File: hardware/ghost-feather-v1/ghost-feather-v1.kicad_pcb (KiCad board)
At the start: 4 copper layers, 72 parts, among them J1 Conn_ARM_SWD_TagConnect_TC2030, J2 USB_C_Receptacle_USB2.0, J3 Conn_01x03, J4 Conn_01x03, J5 Conn_01x03, J6 Conn_01x03, J7 Conn_01x08, Q1 BSS138, Q2 BSS138, Q3 BSS138, Q4 BSS138, SW2 BOOT0, U1 STM32F722RETx, U2 BMI270, U3 USBLC6-2SC6_MOD, U4 MPM3610, U5 MPM3610, X1 16MHz, X2 32kHz768

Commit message: feat: Components placement on PCB #2
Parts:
- moved J5 99.0 mm to (177.0, 53.8)
- moved J6 93.3 mm to (106.7, 57.7)
- moved C14 81.1 mm to (108.0, 53.3)
- moved C17 80.3 mm to (108.7, 124.5)
- moved J4 76.5 mm to (170.5, 130.1)
- moved Q4 68.7 mm to (114.6, 58.2)
- moved R8 68.4 mm to (178.6, 57.7)
- moved Q1 66.4 mm to (113.5, 124.5)
- moved C18 61.1 mm to (118.4, 66.5)
- moved R5 60.3 mm to (110.7, 54.1)
- moved C19 59.0 mm to (121.9, 66.8)
- moved R17 57.0 mm to (105.9, 97.8)
- moved D2 56.3 mm to (124.7, 75.9)
- moved R14 56.3 mm to (108.5, 121.2)
- moved C10 56.2 mm to (125.7, 106.9)
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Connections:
- U1 pad 35: /RF_CH5 -> /RF_CH0
- U1 pad 36: /RF_CH4 -> /RF_CH1
- U1 pad 37: /RF_CH0 -> /RF_CH2
- U1 pad 38: /RF_CH1 -> /RF_CH3
- U1 pad 39: /RF_CH2 -> /RF_CH4
- U1 pad 40: /RF_CH3 -> /RF_CH5

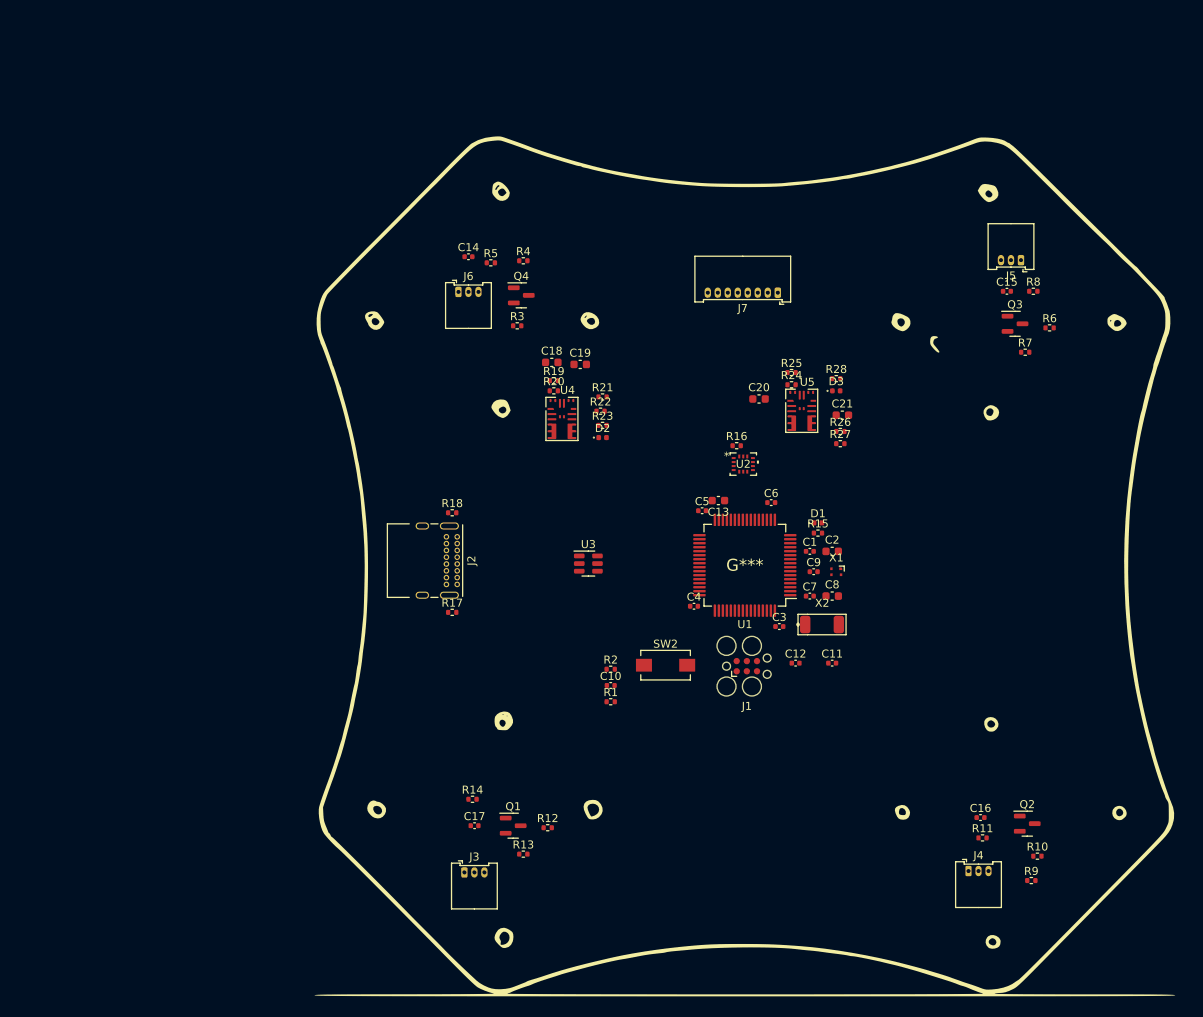
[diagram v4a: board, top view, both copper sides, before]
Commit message: feat: Components placement on PCB #3
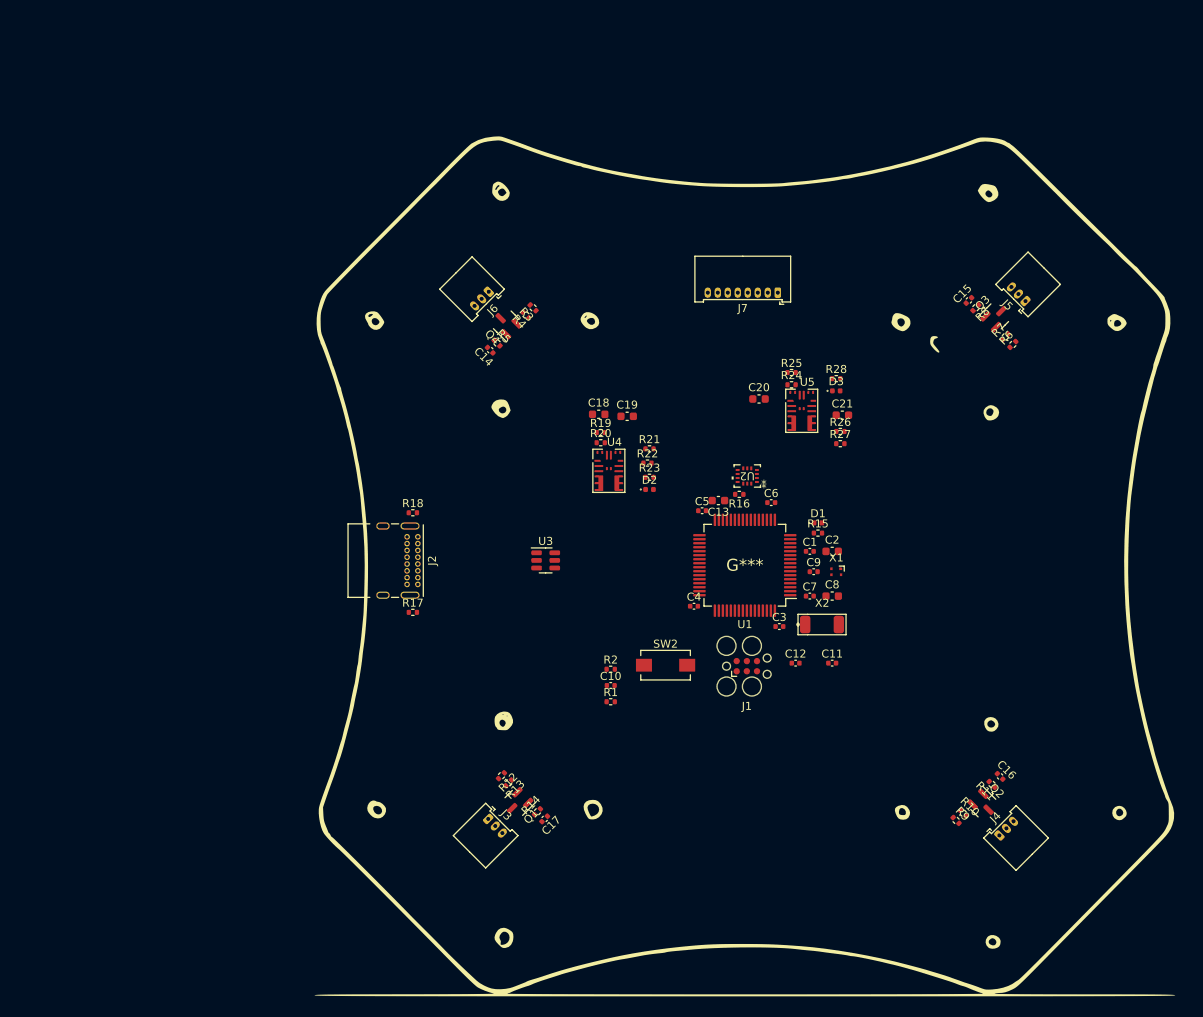
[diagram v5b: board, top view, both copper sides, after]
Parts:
- moved R9 12.0 mm to (168.9, 123.8), turned to -45 degrees
- moved C14 12.0 mm to (110.7, 65.0), turned to 135 degrees
- moved R10 10.7 mm to (169.8, 122.9), turned to -45 degrees
- moved R5 10.1 mm to (111.5, 64.1), turned to -45 degrees
- moved R13 9.09 mm to (113.0, 119.1), turned to -135 degrees
- moved C17 8.81 mm to (117.5, 123.6), turned to -135 degrees
- moved D2 8.75 mm to (130.6, 82.4)
- moved R21 8.75 mm to (130.6, 77.4)
- moved R23 8.75 mm to (130.6, 80.9)
- moved C18 8.75 mm to (124.2, 73.0)
- moved R20 8.75 mm to (124.5, 76.6)
- moved U4 8.75 mm to (125.5, 80.4)
- moved C19 8.75 mm to (127.8, 73.3)
- moved R19 8.75 mm to (124.5, 75.3)
- moved R22 8.75 mm to (130.3, 79.1)
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
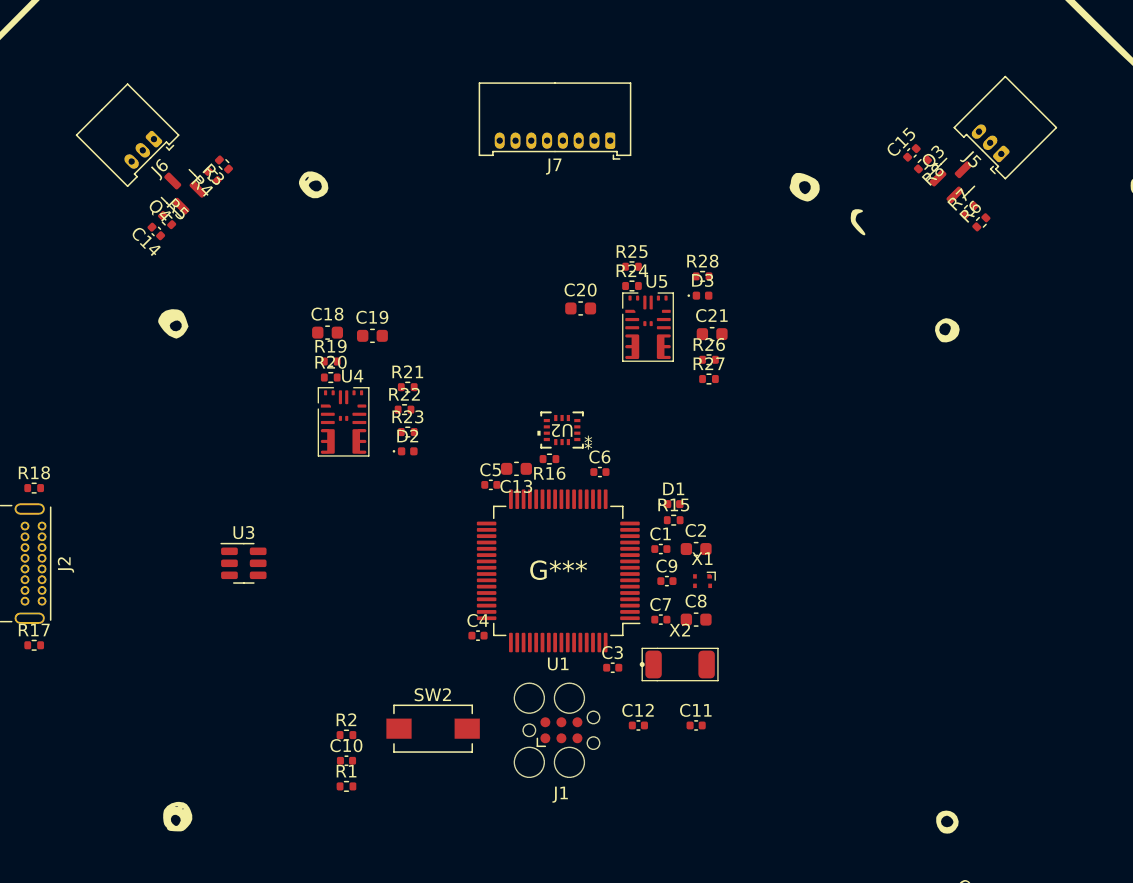
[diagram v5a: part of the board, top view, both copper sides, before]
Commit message: feat: Components placement on PCB #4
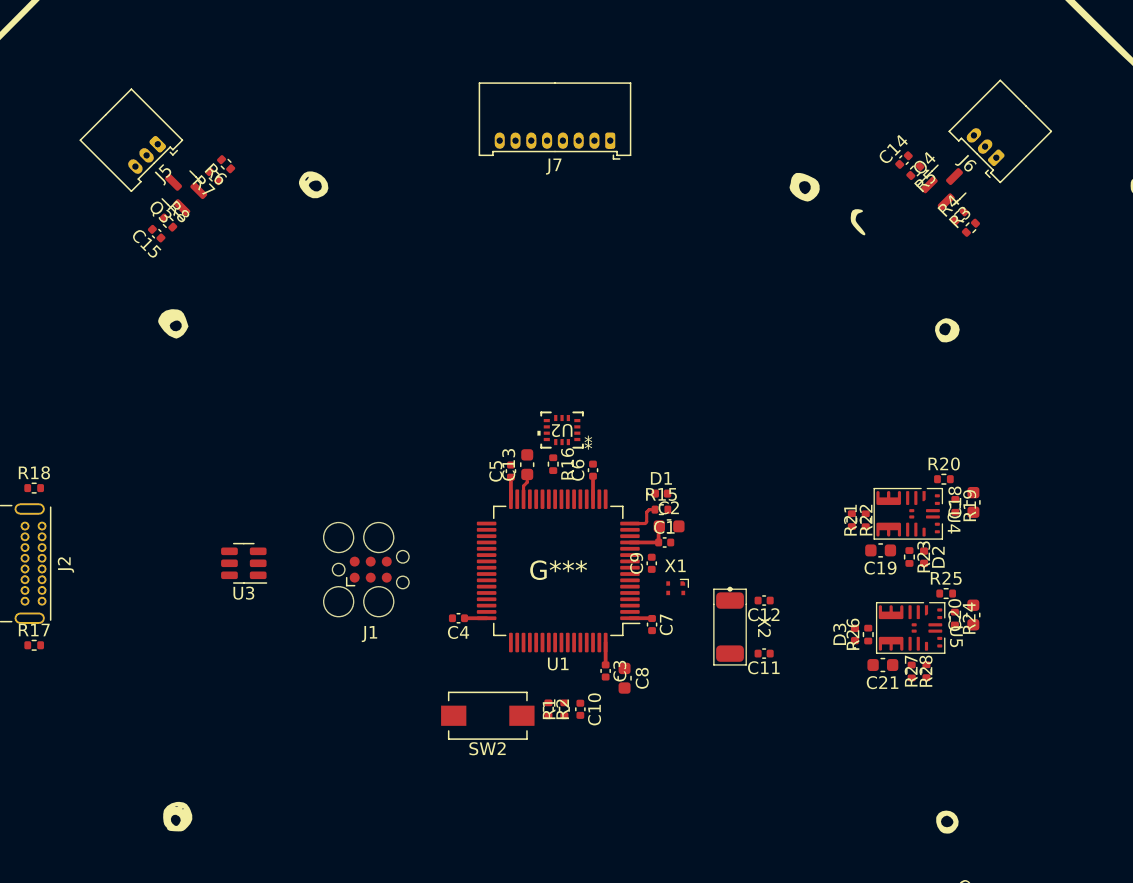
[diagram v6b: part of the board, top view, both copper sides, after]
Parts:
- moved J5 66.8 mm to (110.8, 58.1), turned to -135 degrees
- moved J6 66.7 mm to (177.2, 59.2), turned to 135 degrees
- moved Q3 61.2 mm to (112.7, 61.8), turned to 135 degrees
- moved Q4 60.6 mm to (173.2, 61.3), turned to 45 degrees
- moved C15 60.1 mm to (110.7, 65.2), turned to 135 degrees
- moved R6 60.0 mm to (116.2, 59.7), turned to 135 degrees
- moved R8 59.9 mm to (111.6, 64.3), turned to -45 degrees
- moved R7 59.9 mm to (115.2, 60.6), turned to 135 degrees
- moved C14 59.5 mm to (169.9, 59.4), turned to 45 degrees
- moved R5 59.4 mm to (170.8, 60.2), turned to -135 degrees
- moved R3 59.4 mm to (175.2, 64.7), turned to 45 degrees
- moved R4 59.2 mm to (174.3, 63.8), turned to 45 degrees
- moved C18 52.9 mm to (175.4, 86.5), turned to 90 degrees
- moved R19 50.8 mm to (173.9, 86.8), turned to -90 degrees
- moved R20 49.2 mm to (173.0, 84.6)
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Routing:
- net +3V3: track 0.00 -> 12.4 mm
- net /LED_USER: track 0.00 -> 2.89 mm
- net Net-(U1-VCAP_1): track 0.00 -> 2.08 mm

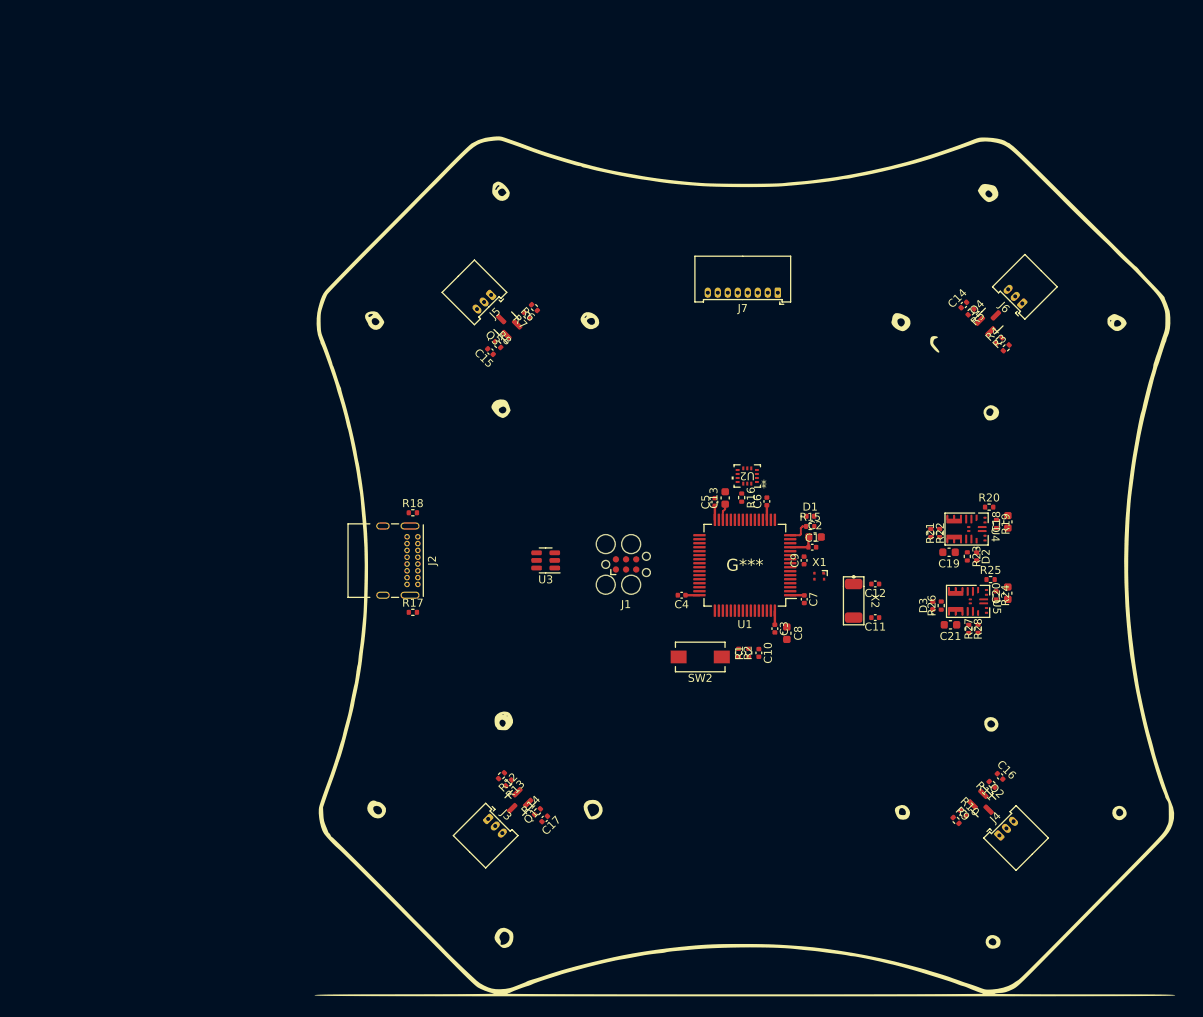
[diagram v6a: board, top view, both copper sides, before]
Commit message: feat: Add the PCB edge cut layer
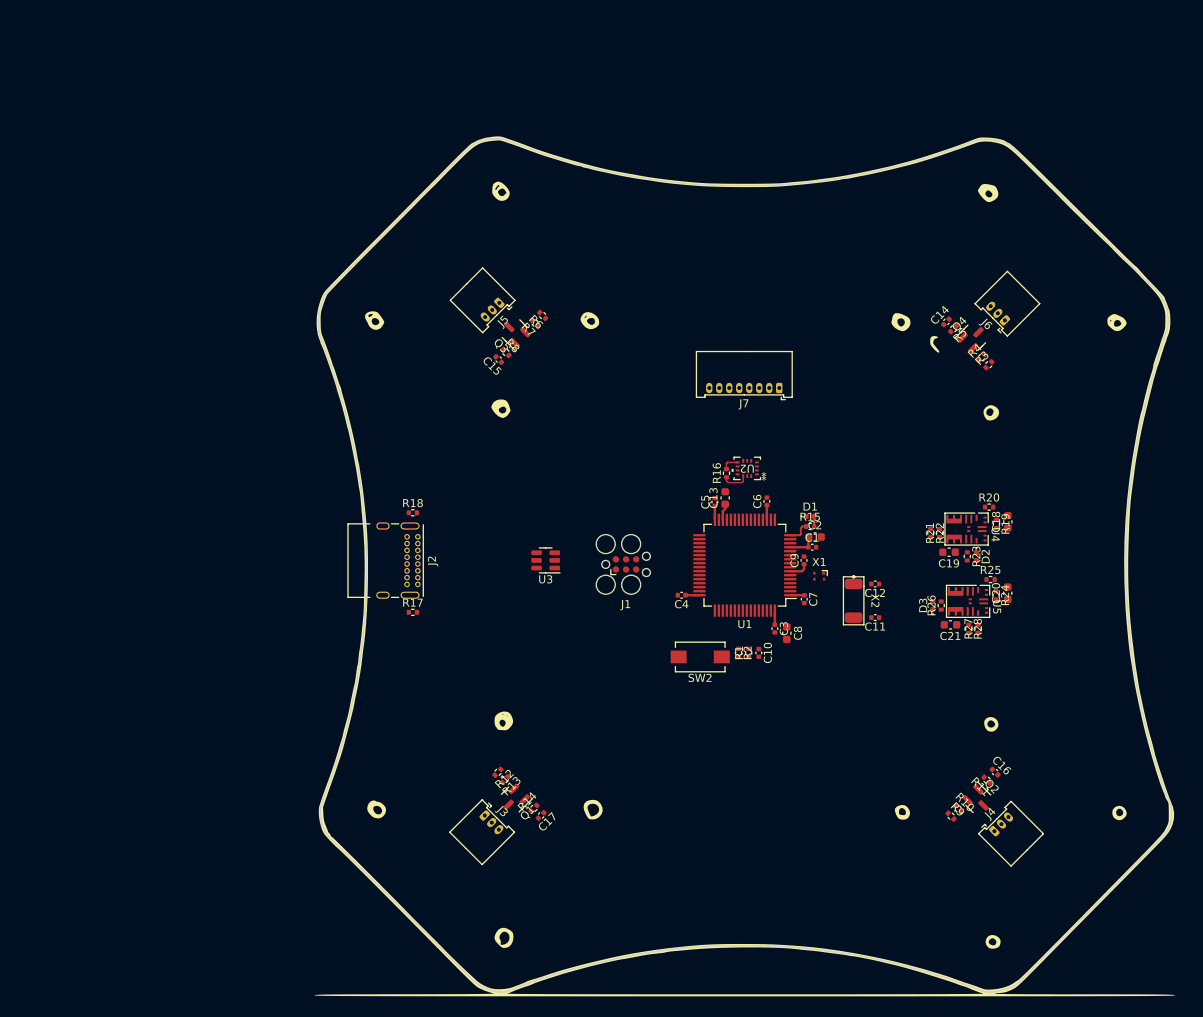
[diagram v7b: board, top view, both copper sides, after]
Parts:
- moved J7 11.9 mm to (146.8, 69.8)
- moved R16 3.59 mm to (140.2, 80.4), turned to 90 degrees
- moved R5 3.03 mm to (168.6, 62.3)
- moved C14 3.03 mm to (167.7, 61.5)
- moved J6 3.03 mm to (175.0, 61.3)
- moved Q4 3.03 mm to (171.0, 63.4)
- moved R3 3.03 mm to (173.0, 66.8)
- moved R4 3.03 mm to (172.1, 65.9)
- moved R8 1.43 mm to (112.6, 65.3)
- moved Q3 1.43 mm to (113.7, 62.8)
- moved R6 1.43 mm to (117.2, 60.7)
- moved R7 1.43 mm to (116.3, 61.6)
- moved C15 1.43 mm to (111.7, 66.2)
- moved J5 1.43 mm to (111.8, 59.1)
- moved U2 0.95 mm to (142.8, 79.8)
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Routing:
- net /BMI270_CSB: track 0.00 -> 3.36 mm
- net /SWD_NRST: track 0.00 -> 2.44 mm
- net +3V3: track 12.4 -> 14.6 mm
- net Net-(D1-A): track 0.00 -> 1.28 mm
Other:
- board outline added: 106.6 x 106.7 mm

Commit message: feat: PCB routing #1
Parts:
- J2: footprint Connector_USB:USB_C_Receptacle_GCT_USB4085 -> Connector_USB:USB_C_Receptacle_GCT_USB4105-xx-A_16P_TopMnt_Horizontal
- moved R27 9.08 mm to (171.6, 108.9)
- moved C20 9.08 mm to (175.3, 104.5)
- moved C21 9.08 mm to (168.2, 108.4)
- moved D3 9.08 mm to (166.0, 106.0)
- moved R24 9.08 mm to (173.9, 104.8)
- moved R25 9.08 mm to (173.2, 102.8)
- moved R26 9.08 mm to (167.0, 106.0)
- moved R28 9.08 mm to (170.5, 108.9)
- moved U5 9.08 mm to (170.1, 105.5)
- moved C18 5.13 mm to (175.5, 81.3)
- moved C19 5.13 mm to (168.1, 85.2)
- moved D2 5.13 mm to (171.6, 85.7)
- moved R19 5.13 mm to (174.0, 81.6)
- moved R20 5.13 mm to (173.1, 79.5)
- moved R21 5.13 mm to (166.9, 82.8)
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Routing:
- net /ESC2: track 0.00 -> 58.8 mm, vias 0 -> 2
- net /ESC3: track 0.00 -> 46.9 mm, vias 0 -> 2
- net /ESC0: track 0.00 -> 40.4 mm, vias 0 -> 2
- net GND: track 0.00 -> 39.0 mm, vias 0 -> 52
- net /ESC1: track 0.00 -> 38.0 mm, vias 0 -> 2
- net /RF_CH0: track 0.00 -> 28.5 mm
- net /RF_CH1: track 0.00 -> 28.4 mm
- net /RF_CH2: track 0.00 -> 28.3 mm
- net /RF_CH3: track 0.00 -> 28.2 mm
- net /RF_CH4: track 0.00 -> 28.0 mm
- net /RF_CH5: track 0.00 -> 27.9 mm
- net /OSC32_IN: track 0.00 -> 13.7 mm
- net /OSC32_OUT: track 0.00 -> 10.2 mm
- net /SPI1_SCK: track 0.00 -> 8.24 mm, vias 0 -> 2
- net /SPI1_MISO: track 0.00 -> 7.90 mm
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- added copper zone on B.Cu, net GND
